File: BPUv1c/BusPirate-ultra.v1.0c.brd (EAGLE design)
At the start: 100 x 50 mm, 198 parts, among them J1 USB-C-12, J2 CON_HEADER_1X04, J3 CON_HEADER_1X10-RIGHT_ANGLED_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, J4 CON_MOLEX_MALE_SMT_SH_1.25, Q300 PMV65XP, Q301 DMMT3906W, U100 STM32F103ZX, U101 W25X40CL, U200 74HCT4067, U201 MCP6001, U202 ADS7041, U300 MCP1824_ADJ, U301 MCP6001, U302 MCP1700, U303 MCP1801T-1202I/OT, U400 SN74LVC1T45DBV, U401 SN74LVC1T45DBV, U402 74LVC1G07DBV, U403 74LVC1G07DBV, U404 SN74LVC1T45DBV, U405 SN74LVC1T45DBV, U406 74LVC1G07DBV, U407 74LVC1G07DBV, U408 SN74LVC1T45DBV, U409 SN74LVC1T45DBV, U410 74LVC1G07DBV, U411 74LVC1G07DBV, U412 SN74LVC1T45DBV, U413 SN74LVC1T45DBV, U414 74LVC1G07DBV, U415 74LVC1G07DBV, U500 74HCT4066PW, U501 74HCT4066PW, U600 23LC1024, U601 23LC1024, U602 74LVC245A, U700 ICE40HX4K

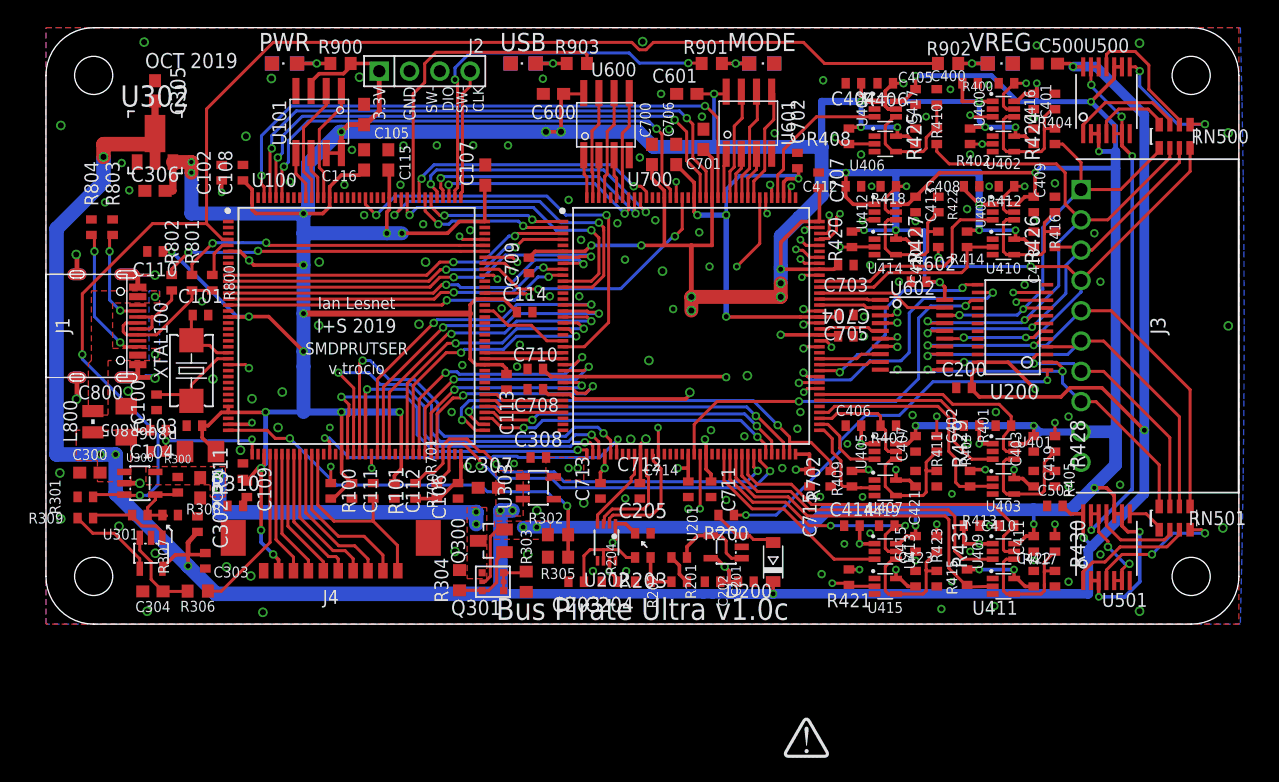
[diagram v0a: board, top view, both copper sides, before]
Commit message: change display connector to FPC connector, done routing
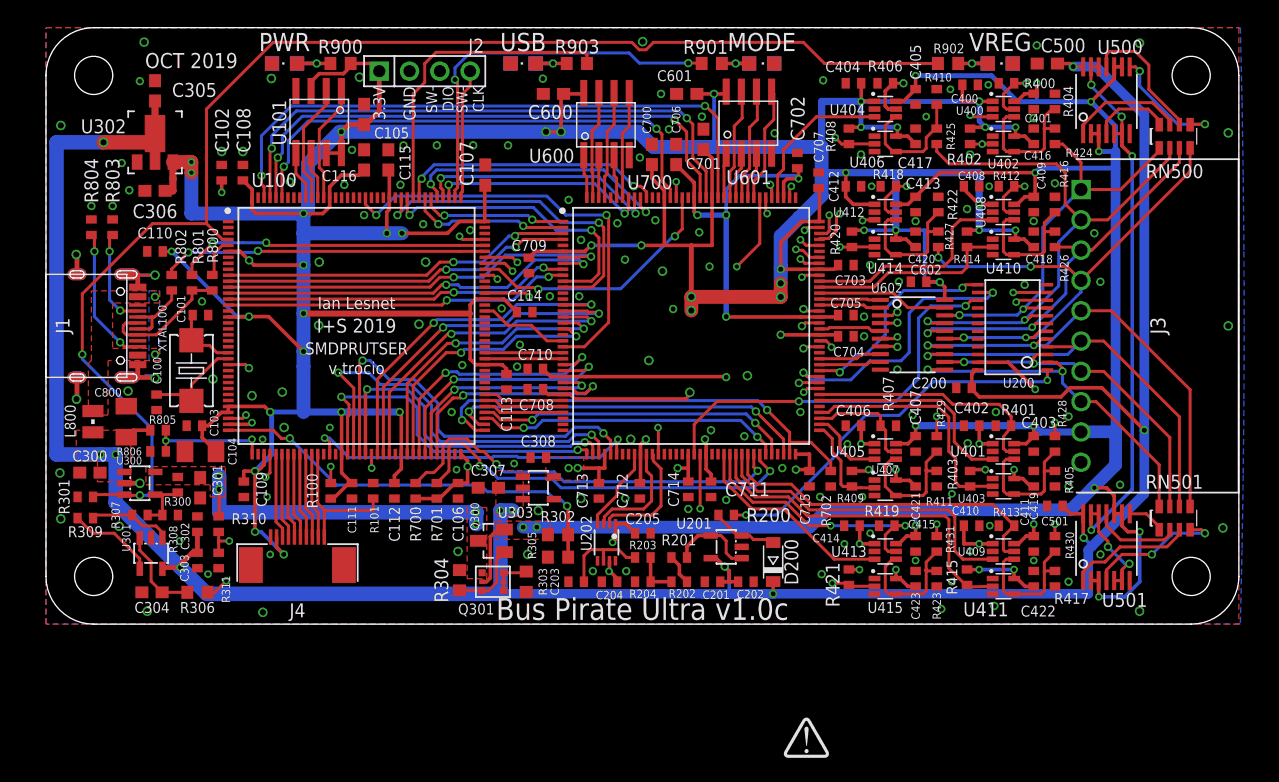
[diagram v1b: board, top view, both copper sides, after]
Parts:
- J4: value CON_MOLEX_MALE_SMT_SH_1.25 -> CON-FPC_X05B20L10T; device dp_devices.v6:MOLEX_533980771 -> dp_devices.v6:X05B20L10T
- moved R311 7.76 mm to (14.5, 5.33), turned to 270 degrees
- moved J4 2.90 mm to (21.1, 4.95)
- moved R310 2.07 mm to (14.5, 8.38), turned to 270 degrees
- moved C303 0.66 mm to (12.7, 5.33)
- moved C109 0.25 mm to (16.6, 11.3)
- moved C713 0.13 mm to (46.4, 11.2)
- moved C400 0.13 mm to (77.5, 45.2)
- moved C304 0.11 mm to (8.89, 2.67)
- moved R306 0.10 mm to (12.7, 2.67)
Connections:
- net 3V3: now also J4.9; no longer J4.P9
- net DISPLAY_AUX1: now also J4.2; no longer J4.P2
- net DISPLAY_CS: now also J4.5; no longer J4.P5
- net DISPLAY_D/P: now also J4.4; no longer J4.P4
- net DISPLAY_PWM: now also J4.3; no longer J4.P3
- net DISPLAY_RESET: now also J4.1; no longer J4.P1
- net DISPLAY_SPI_CLOCK: now also J4.8; no longer J4.P8
- net DISPLAY_SPI_MISO: now also J4.7; no longer J4.P7
- net DISPLAY_SPI_MOSI: now also J4.6; no longer J4.P6
- net GND: now also J4.10; no longer J4.P10
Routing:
- net MCU_ADC0: track 0.00 -> 15.5 mm, vias 0 -> 2
- net DISPLAY_AUX1: track 13.5 -> 7.17 mm
- net DISPLAY_PWM: track 12.7 -> 7.17 mm
- net DISPLAY_D/P: track 12.2 -> 7.17 mm
- net DISPLAY_CS: track 11.7 -> 7.17 mm
- net DISPLAY_RESET: track 16.6 -> 12.4 mm
- net DISPLAY_SPI_MOSI: track 11.0 -> 7.17 mm
- net DISPLAY_SPI_MISO: track 10.7 -> 7.17 mm
- net DISPLAY_SPI_CLOCK: track 10.4 -> 7.17 mm
- net 1V2: track 115.4 -> 117.7 mm, vias 10 -> 9
- net N$26: track 25.7 -> 28.0 mm
- net N$12: track 5.69 -> 5.00 mm
- net VUSB: track 233.2 -> 233.8 mm
- net VREG_DAC: track 14.3 -> 14.8 mm, vias 0 -> 2
- net 3V3: track 620.1 -> 620.5 mm, vias 64 -> 62
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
